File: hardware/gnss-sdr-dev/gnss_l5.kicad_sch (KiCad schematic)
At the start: 24 parts, among them U301 MAX2771

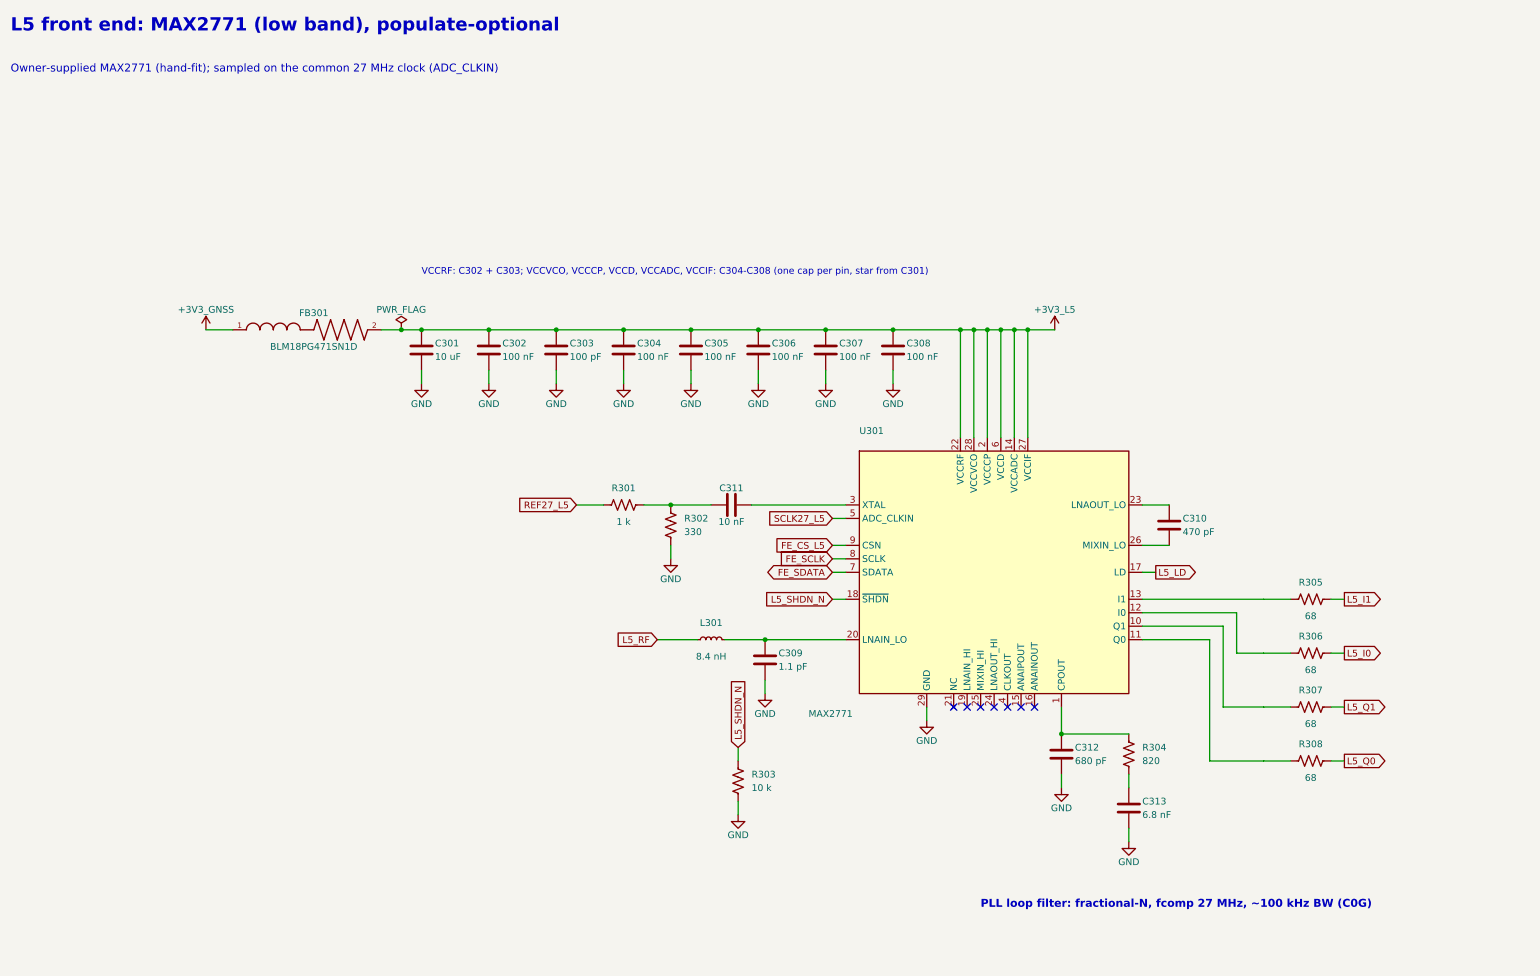
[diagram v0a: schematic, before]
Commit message: hardware(gnss-sdr-dev): L1/L5 decoupling drawn per pin -- each supply pin of the MAX2769B and MAX2771 with its own caps, smallest nearest
As on the FPGA power sheet and the Space Bug P4 sheet: each supply pin's row runs to a
corner (rail label), a spine goes up to a shelf, and that pin's own caps hang there. On
VCC_RF / VCCRF the 100 pF sits nearest the pin, then the 100 nF. The bulk (C201, C301)
stays after its ferrite.

The six supply pins of each chip move to the top of the left side of its symbol (pin
numbers unchanged) and XTAL to the bottom of that side, so the oscillator chain stays
clear of the new rows.

Connectivity is unchanged: 399 nets, the same pin groups; ERC 0 errors. The sheet files all
change because the generator issues fresh UUIDs; there is no layout yet, so nothing is
unlinked.

Co-Authored-By: Claude Opus 5.5 <noreply@anthropic.com>
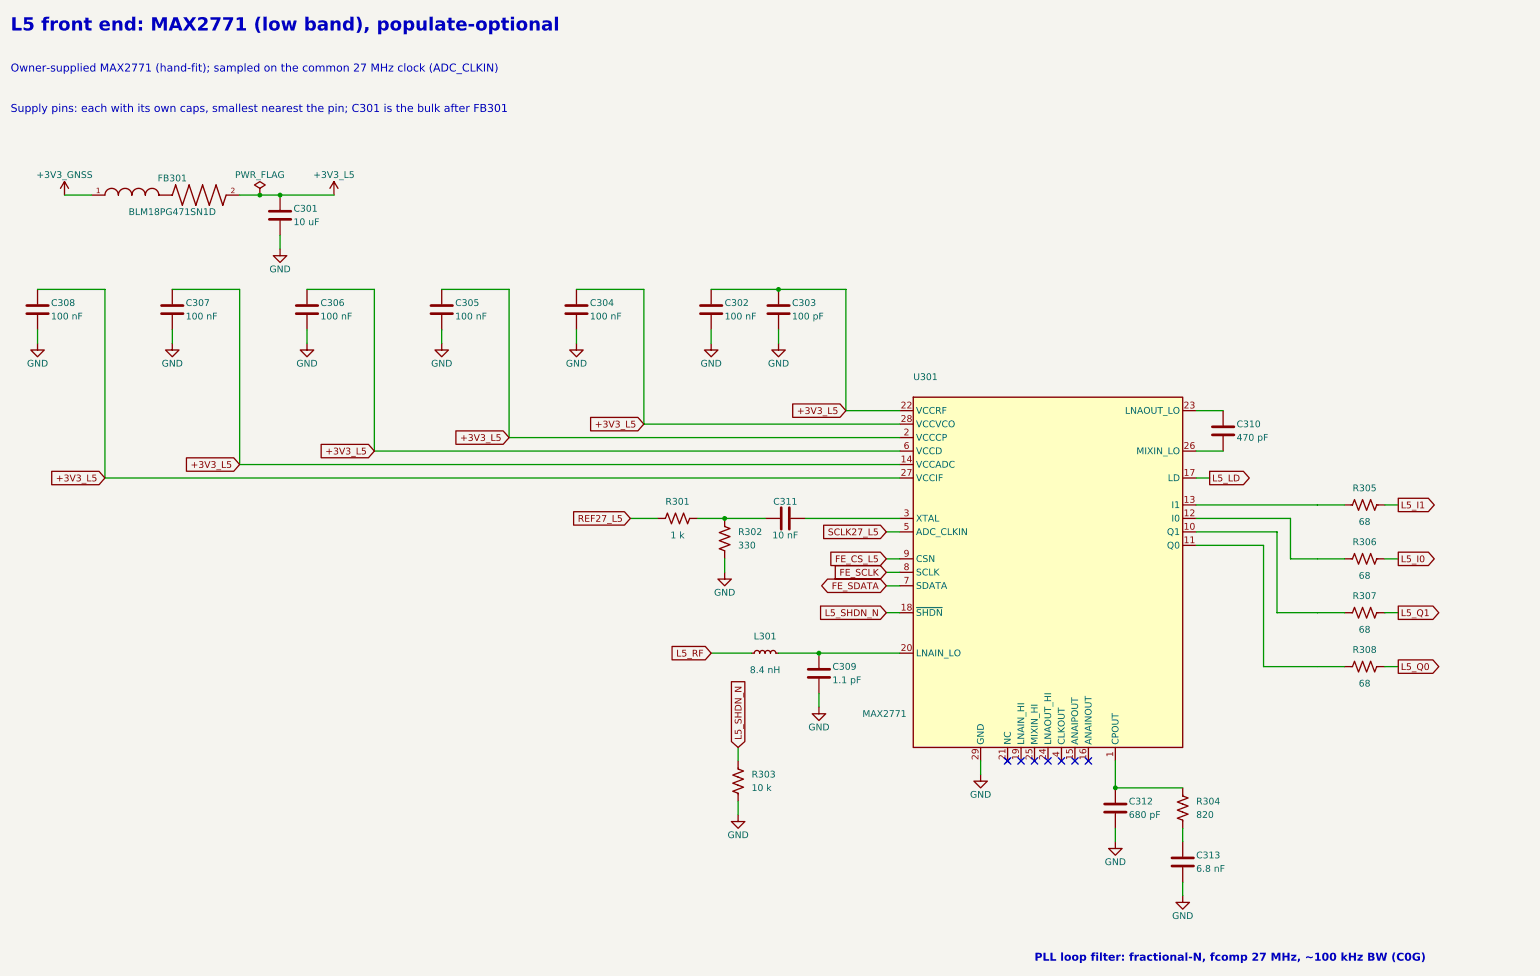
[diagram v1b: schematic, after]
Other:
- note added: "Supply pins: each with its own caps, smallest nearest the pin; C301 is the bulk after FB301"
- note removed: "VCCRF: C302 + C303; VCCVCO, VCCCP, VCCD, VCCADC, VCCIF: C304-C308 (one cap per pin, star from C301)"

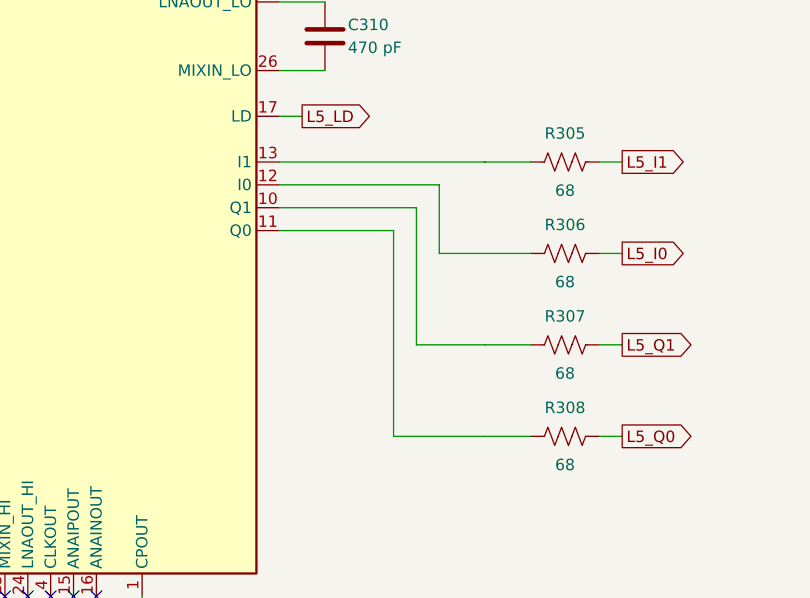
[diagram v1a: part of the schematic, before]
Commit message: hardware(gnss-sdr-dev): eight layers with the P4 wired, a boot button on GPIO35, Mantis design rules, a review pass, 3D models for every part, and the USB-HS pairs re-routed to 90 ohm
Stackup and routing:
- Eight layers on the Beetle's JLC08161H-2116 stack: F signal / In1 GND / In2 signal / In3 GND / In4 power / In5 north-south / In6 east-west / B GND (+1V1 island).
- The P4 cluster is wired (FPGA link, configuration, front-end control, boot flash, NAND, IMU, USB control). With the owner's placement work, nothing is left unconnected.

Boot button (owner: "add a boot button on GPIO35 like the space bug"):
- R15 100 k pulls GPIO35 up to +3V3_MCU. R24 1 k and SW1 (R-667995) pull it to GND, as on the Space Bug.
- The owner placed the parts. It is the only netlist change in the sheets; the rest of the sheet diffs are KiCad re-saves.

Design rules = Tinker-Mantis:
- 0.1 mm net-class clearance; 0.09 mm minimum track; 0.1 mm hole clearance; 0.2 mm hole-to-hole and copper-to-edge.
- Every copper pour keeps its own 0.2 mm clearance, which is the RF lines' ground gap.

Review pass:
- U7/U502 (W25Q128JVYIQ): the vias are moved off the 0.254 mm balls to sit beside them. JLC had queried vias the size of the ball pads. No via now overlaps a ball.
- DRC fixes:
  - the NAND_SCK via that shorted C65 moved;
  - one GND via moved for clearance;
  - C71 nudged off C72's courtyard.
- Ten +3V3 pins and caps tied to the plane; the C47-C49/C67 ground island tied in.
- Vias added:
  - 163 GND return vias beside signal and power vias and at cap grounds;
  - exposed pads: U9 gets 5 vias, U401 gets 12 (both had none).
- ESP_VDD_HP necks at P4 pins 76 and 91 widened from 0.1 to 0.2-0.3 mm.
- X/Y silkscreen letters raised to the 0.8 mm minimum. Dead stubs, duplicate segments and an overlap removed.

3D models:
- KiCad 10 does not ship models for:
  - the TQFN-28 front ends (U201/U301);
  - the TG2520SMN TCXO (Y201);
  - the Laird BMI-S-205 shield (SH1).
- They are generated with CadQuery from the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
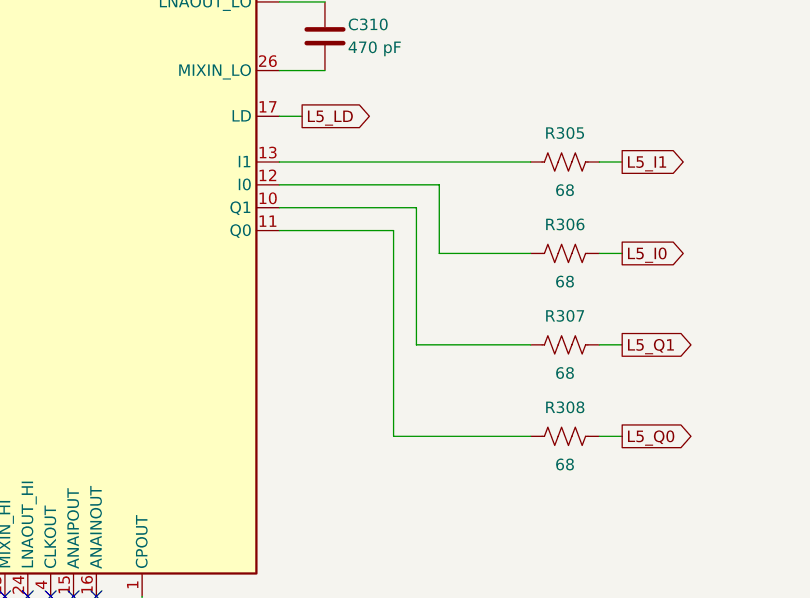
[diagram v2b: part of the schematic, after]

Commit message: hardware(gnss-sdr-dev): the design review's before-assembly fixes -- FL401 a 2 A shielded power-line choke, U601 a 0.5 pF HS ESD array with a VBUS TVS, and the value fixes
The boards were not ordered yet, so the copper can still change. Schematic only: the PCB is not updated yet (the
owner runs Update PCB and places FL401, U601 and the new D602), so DRC parity stays red until then.

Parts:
- FL401: Bourns SRF3225TP-501Y (2 A, 0.1 ohm max, 60 V, 500 ohm at 100 MHz, -40 to +105 C, shielded) replaces the
  DLW21SN670HQ2L, a 320 mA USB data-line choke that carried the whole board's input current. No 0805 choke reaches
  0.8 A. New footprint FIL_SRF3225TP (Bourns layout), a CadQuery model and a Custom symbol.
- U601: TI TPD4E05U06DQAR, 0.5 pF. The ESP32-P4 guide allows 1 pF on the high-speed lines; the USBLC6-2SC6 was
  2.5-3.5 pF. USON-10 with D+ on pins 1 and 10 and D- on 2 and 9, for flow-through routing; channel 2 is unused.
- D602 (new): LESD5D5.0CT1G on VBUS_HS, as on Espressif's ESP32-P4-Function-EV-Board. The new U601 has no VBUS pin.
- C403 2.2 -> 22 nF: the GNSS LDO now ramps after the FPGA rails. The front ends no longer drive the ECP5's left
  banks (not hot-socket rated) while those are unpowered.
- R104 10 -> 2.2 ohm: at least 3.15 V at the antenna at 30 mA, and no overload into a shorted feed.
- R503/R504 1 k -> 0 ohm: the configuration straps Lattice asks for (< 500 ohm).
- FB501 470 -> 120 ohm bead (BLM18PG121SN1D), inside the ECP5 checklist's range.
- C105 1 -> 100 nF (the BGA524N6 asks for > 10 nF); C408 1 -> 2.2 uF on the LP5907 output.
- U301 (MAX2771) marked do-not-fit: owner stock, fitted by hand.
- U701's Datasheet field now points at the GD5F2GQ5UE datasheet.
- FABRICATION-NOTES.md: U8 joins the parts with no pin-1 mark, U301 joins the do-not-fit list, and the U9 sentence is
  corrected (U9 makes +3V3_MCU; the FPGA core buck is U403).

ERC: 0 errors and the same 15 warnings. The netlist changes only for the parts above.

The bring-up and firmware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
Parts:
- U301: now not fitted
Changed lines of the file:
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@@
 		(on_board yes)
 		(in_pos_files yes)
-		(dnp no)
+		(dnp yes)
 		(fields_autoplaced yes)
 		(property "Reference" "U301"

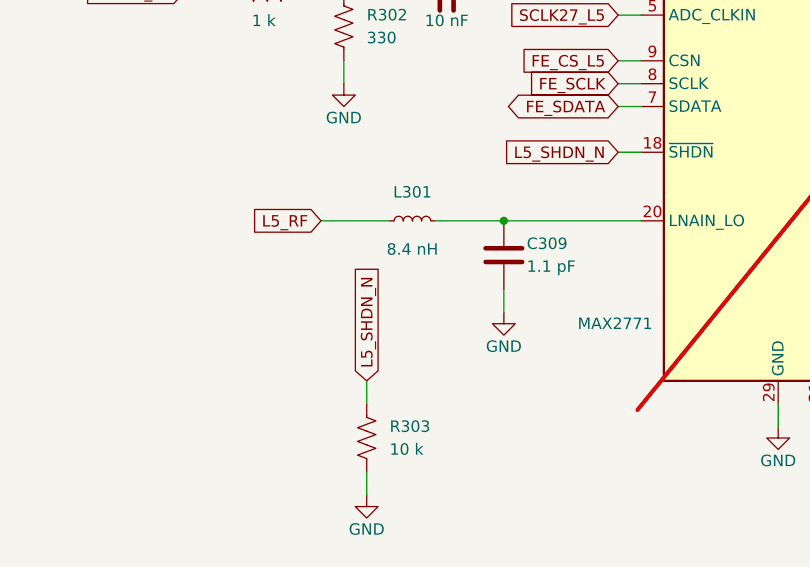
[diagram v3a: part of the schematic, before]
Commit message: hardware: the 1 uF 0402 caps consolidate on the 16 V CL05A105KO5NNNC, with the pending part and layout work
Every GRM155R61A105KE15D (Murata, 10 V X5R) becomes the Samsung CL05A105KO5NNNC (16 V X5R) on
space-bug-m8t, gnss-sdr-dev and the legacy gnss-px1105r board -- 34 symbols and their 34 footprints.
Same 0402 footprint, so only the MPN and Mfr change. The higher-rated part is already the 1 uF used
on the Tinker boards, so the BOMs now carry one 1 uF line instead of two.

Pending work committed alongside:
- space-bug-m8t: the 10 uF bulk caps go to CL21A226MOQNNNE, added CL05A106MQ5NUNC, RC0402FR-071KL and
  R-667995 parts, schematic, layout and DRC rule updates, and the new FABRICATION-NOTES.md
- gnss-sdr-dev: the 5.1 nH inductors go from LQG15HS5N1S02D to LQW15AN5N1C00D, added 1 k and 100 k
  resistors, and schematic and layout updates
- legacy gnss-px1105r: the 10 uF caps go to CL21A226MOQNNNE, plus schematic and layout updates
- tinker-beetle: the 390 pF caps go to GRM1555C1H391JA01D, the 100 k resistors to RC0402FR-07100KL,
  and the 2.2 uH inductor from XGL4020-222ME to SRP4020FA-2R2M
- gnss-sam10m8-18mm-hv: the 100 pF cap goes from CL05C101JB5NNNC to GRM1555C1H101JA01D
- the Taoglas CGGBP.25.4.A.02 antenna footprint, and project-file housekeeping

Co-Authored-By: Claude Opus 5.5 <noreply@anthropic.com>
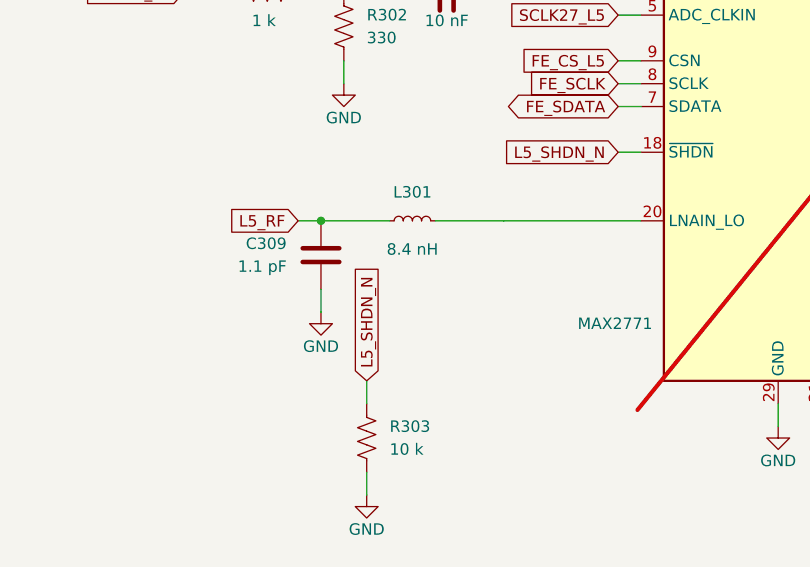
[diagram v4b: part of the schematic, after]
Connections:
- net L5_RF: now also C309.1
- net at L301.2, U301.20 (LNAIN_LO): no longer C309.1
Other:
- moved on the sheet: C309
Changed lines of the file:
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@@
 		(color 0 0 0 0)
 	)
-	(junction
-		(at 172.72 142.24)
-		(diameter 0)
-		(color 0 0 0 0)
-	)
 	(no_connect
 		(at 213.36 162.56)
@@
 	(wire
 		(pts
-			(xy 172.72 149.86) (xy 172.72 152.4)
-		)
-		(stroke
-			(width 0)
-			(type default)
-		)
-	)
-	(wire
-		(pts
 			(xy 76.2 73.66) (xy 88.9 73.66)
 		)
@@
 	(wire
 		(pts
-			(xy 152.4 142.24) (xy 160.02 142.24)
-		)
-		(stroke
-			(width 0)
-			(type default)
-		)
-	)
-	(wire
-		(pts
 			(xy 185.42 129.54) (xy 187.96 129.54)
 		)
@@
 	(global_label "L5_RF"
 		(shape input)
-		(at 152.4 142.24 180)
+		(at 149.86 142.24 180)
 		(fields_autoplaced yes)
 		(effects
@@
 		)
 		(property "Intersheetrefs" "${INTERSHEET_REFS}"
-			(at 152.4 142.24 0)
+			(at 149.86 142.24 0)
 			(hide yes)
 			(show_name no)
@@
 	(symbol
 		(lib_id "power:GND")
-		(at 172.72 152.4 0)
+		(at 152.4 152.4 0)
 		(unit 1)
 		(body_style 1)
@@
 		(fields_autoplaced yes)
 		(property "Reference" "#PWR_L5 receiver_13"
-			(at 172.72 158.75 0)
+			(at 152.4 158.75 0)
 			(hide yes)
 			(show_name no)
@@
 		)
 		(property "Value" "GND"
-			(at 172.72 156.21 0)
+			(at 152.4 156.21 0)
 			(show_name no)
 			(do_not_autoplace no)
@@
 		)
 		(property "Footprint" ""
-			(at 172.72 152.4 0)
+			(at 152.4 152.4 0)
 			(hide yes)
 			(show_name no)
@@
 		)
 		(property "Datasheet" ""
-			(at 172.72 152.4 0)
+			(at 152.4 152.4 0)
 			(hide yes)
 			(show_name no)
@@
 		)
 		(property "Description" ""
-			(at 172.72 152.4 0)
+			(at 152.4 152.4 0)
 			(hide yes)
 			(show_name no)
@@
 	(symbol
 		(lib_id "Device:C")
-		(at 172.72 146.05 0)
+		(at 152.4 146.05 0)
 		(unit 1)
 		(body_style 1)
@@
 		(fields_autoplaced yes)
 		(property "Reference" "C309"
-			(at 175.26 144.78 0)
+			(at 148.59 144.78 0)
 			(show_name no)
 			(do_not_autoplace no)
@@
 					(size 1.27 1.27)
 				)
-				(justify left)
+				(justify right)
 			)
 		)
 		(property "Value" "1.1 pF"
-			(at 175.26 147.32 0)
+			(at 148.59 147.32 0)
 			(show_name no)
 			(do_not_autoplace no)
@@
 					(size 1.27 1.27)
 				)
-				(justify left)
+				(justify right)
 			)
 		)
 		(property "Footprint" "Capacitor_SMD:C_0402_1005Metric"
-			(at 172.72 146.05 0)
+			(at 152.4 146.05 0)
 			(hide yes)
 			(show_name no)
@@
 		)
 		(property "Datasheet" ""
-			(at 172.72 146.05 0)
+			(at 152.4 146.05 0)
 			(hide yes)
 			(show_name no)
@@
 		)
 		(property "Description" "Capacitor 1.1 pF C0G +-0.05 pF"
-			(at 172.72 146.05 0)
+			(at 152.4 146.05 0)
 			(hide yes)
 			(show_name no)
@@
 		)
 		(property "MPN" "GJM1555C1H1R1WB01D"
-			(at 172.72 146.05 0)
+			(at 152.4 146.05 0)
 			(hide yes)
 			(show_name no)
@@
 		)
 		(property "Mfr" "Murata"
-			(at 172.72 146.05 0)
+			(at 152.4 146.05 0)
 			(hide yes)
 			(show_name no)
@@
 		)
 	)
+	(wire
+		(pts
+			(xy 149.86 142.24) (xy 152.4 142.24)
+		)
+		(stroke
+			(width 0)
+			(type default)
+		)
+	)
+	(wire
+		(pts
+			(xy 152.4 142.24) (xy 160.02 142.24)
+		)
+		(stroke
+			(width 0)
+			(type default)
+		)
+	)
+	(junction
+		(at 152.4 142.24)
+		(diameter 0)
+		(color 0 0 0 0)
+	)
+	(wire
+		(pts
+			(xy 152.4 149.86) (xy 152.4 152.4)
+		)
+		(stroke
+			(width 0)
+			(type default)
+		)
+	)
